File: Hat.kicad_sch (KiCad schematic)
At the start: 57 parts, among them J0 SPI0, J1 X_UART_RPI0, J2 X_UART_MCU0, J3 X_ALIM0, U0 PCA9517D

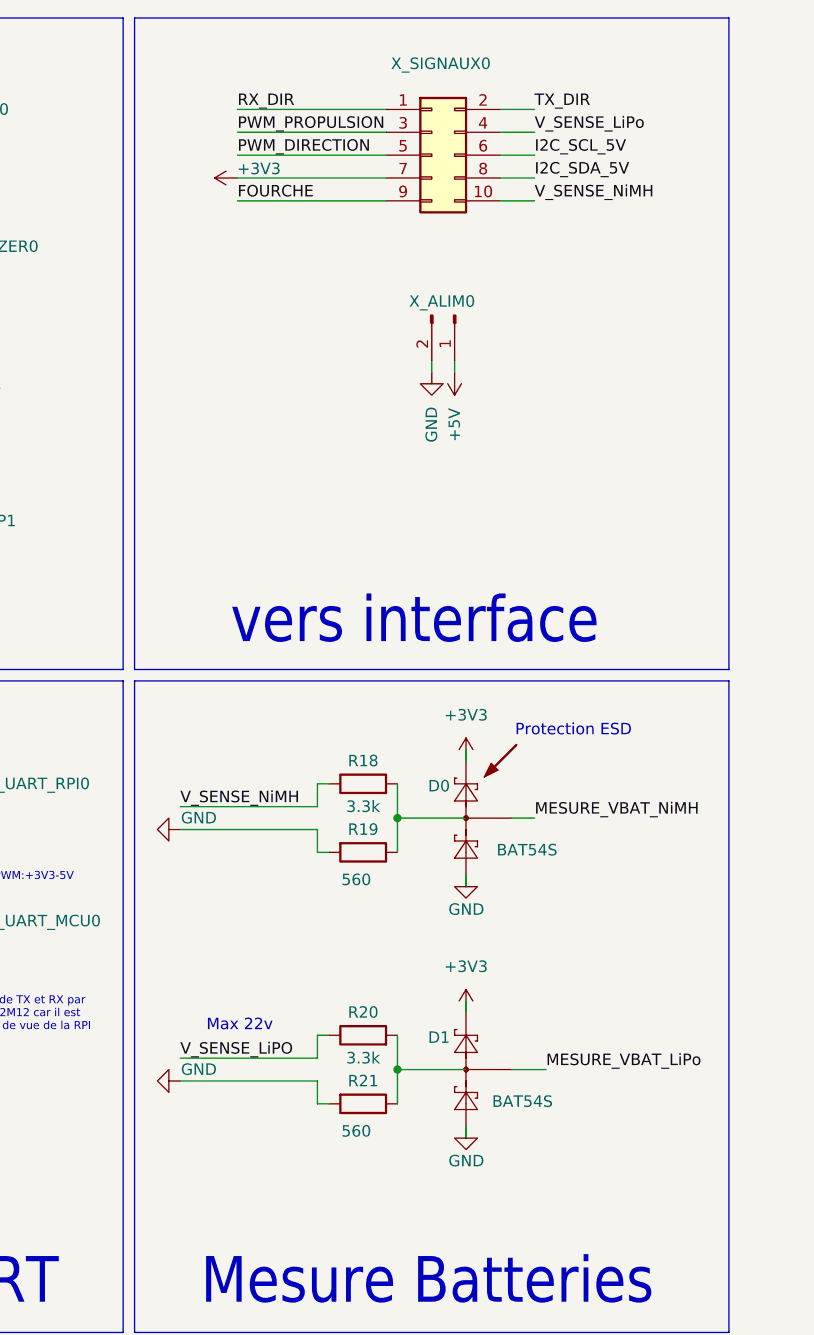
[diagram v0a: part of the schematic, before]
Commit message: added gnd to signals connector
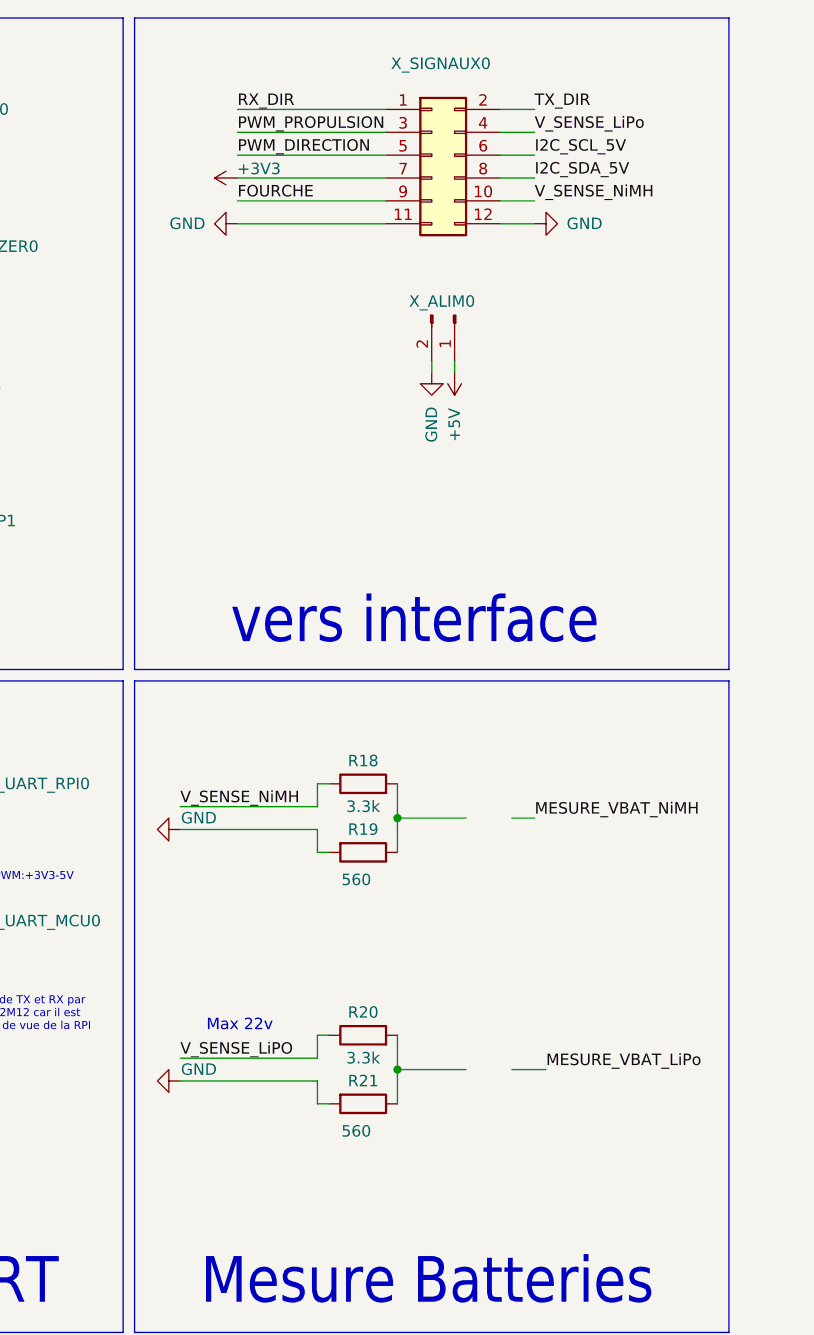
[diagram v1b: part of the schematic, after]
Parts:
- removed D0, D1: BAT54S, Package_TO_SOT_SMD:SOT-23, symbol Diode:BAT54S
- J3: footprint (none) -> Connector_AMASS:AMASS_XT30PW-M_1x02_P2.50mm_Horizontal
- X_MEZZANINE0: value ~ -> (none)
- X_SIGNAUX0: footprint Connector_IDC:IDC-Header_2x05_P2.54mm_Vertical -> Connector_IDC:IDC-Header_2x06_P2.54mm_Vertical; symbol Connector_Generic:Conn_02x05_Odd_Even -> Connector_Generic:Conn_02x06_Odd_Even
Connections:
- net GND: now also X_SIGNAUX0.11 (Pin_11), X_SIGNAUX0.12 (Pin_12)
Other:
- note removed: "Protection ESD"
